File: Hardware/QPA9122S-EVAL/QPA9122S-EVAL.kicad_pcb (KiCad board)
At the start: 2 copper layers, 58.5 x 27.9 mm, 15 parts, among them IC1 QPA9122TR7, J1 Conn_Coaxial, J2 Conn_Coaxial

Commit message: Power distribution
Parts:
- added J3: Conn_01x02_Pin, Connector_PinHeader_1.00mm:PinHeader_1x02_P1.00mm_Vertical, F.Cu at (122.2, 83.0)
- added J4: Conn_01x02_Pin, Connector_PinHeader_1.00mm:PinHeader_1x02_P1.00mm_Vertical, F.Cu at (114.9, 107.1)
- added J5: Conn_01x02_Pin, Connector_PinHeader_1.00mm:PinHeader_1x02_P1.00mm_Vertical, F.Cu at (113.8, 83.1)
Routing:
- net V_PD: track 0.00 -> 8.58 mm
- net VCC: track 7.41 -> 15.5 mm
- net VCC1: track 2.81 -> 9.59 mm
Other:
- board text added: "+1.8V"
- board text added: "+5V"
- board text added: "GND"

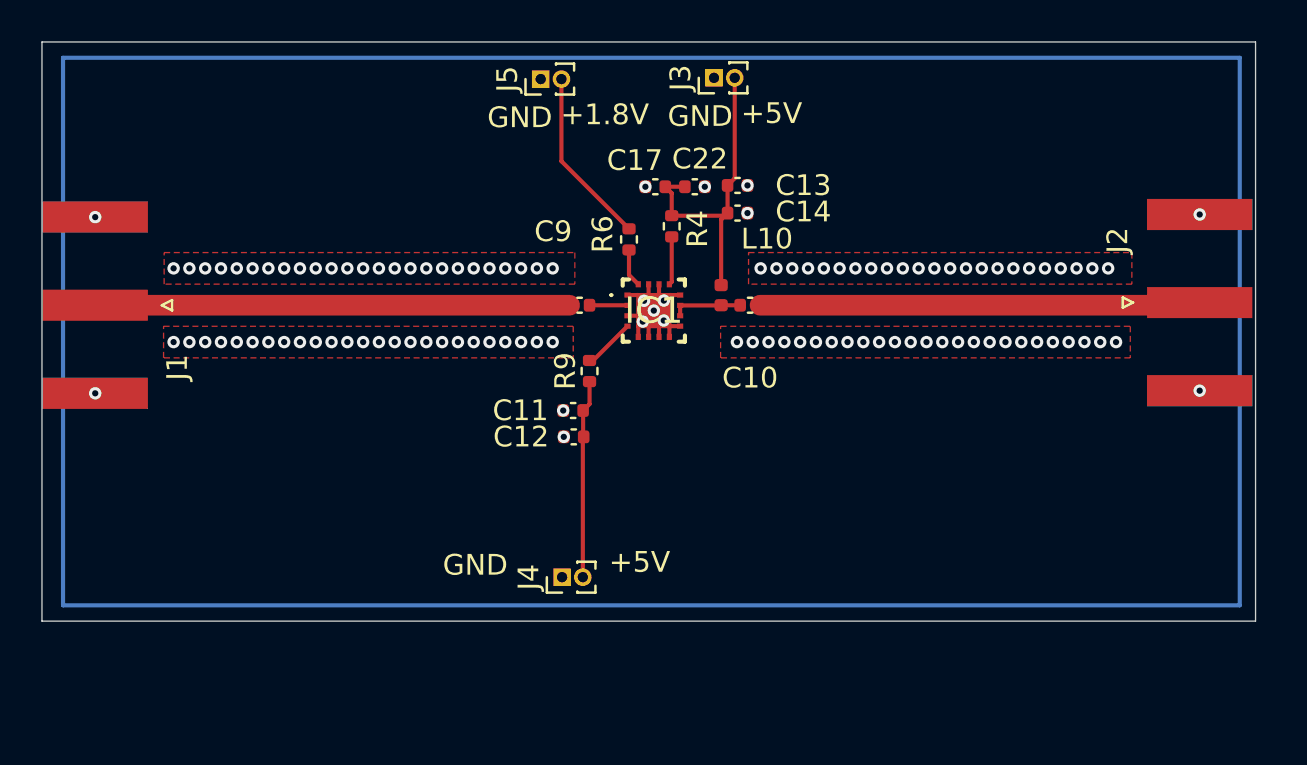
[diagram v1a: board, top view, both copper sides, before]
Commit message: Added T-line test point and better labeling.
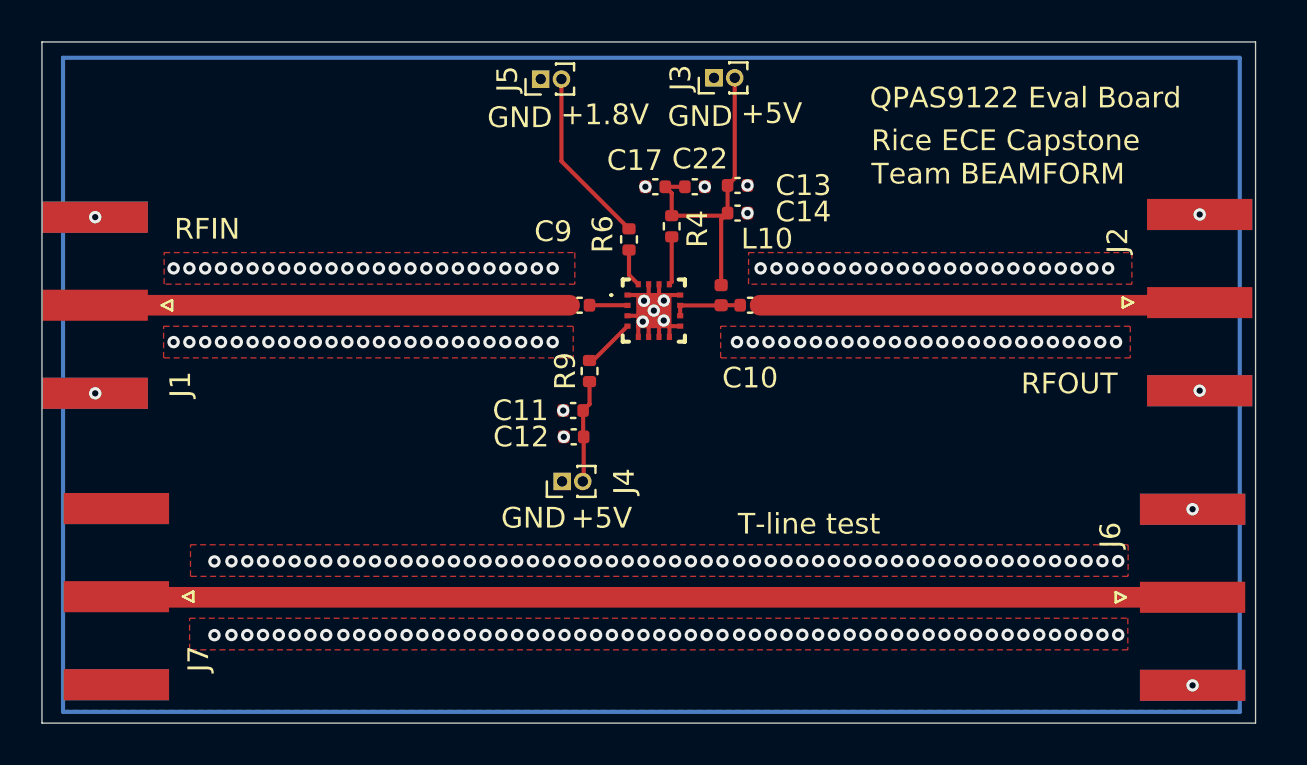
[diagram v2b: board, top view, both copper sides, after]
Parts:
- added J6: Conn_Coaxial, Connector_Coaxial:SMA_Amphenol_132289_EdgeMount, F.Cu at (145.3, 108.1)
- added J7: Conn_Coaxial, Connector_Coaxial:SMA_Amphenol_132289_EdgeMount, F.Cu at (93.4, 108.0)
- moved J4 4.62 mm to (114.9, 102.5)
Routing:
- net Net-(J6-In): track 0.00 -> 51.9 mm
- net VCC1: track 9.59 -> 5.03 mm
- net GND: vias 113 -> 231
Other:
- board size 58.5 x 27.9 mm -> 58.5 x 32.9 mm
- board text added: "QPAS9122 Eval Board"
- board text added: "RFIN"
- board text added: "RFOUT"
- board text added: "Rice ECE Capstone Team BEAMFORM"
- board text added: "T-line test"

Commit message: DRC fixes
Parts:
- moved J1 0.63 mm to (93.0, 94.0)
- moved J2 0.44 mm to (145.2, 93.9)
- moved J6 0.16 mm to (145.1, 108.1)
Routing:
- net GND: vias 231 -> 233
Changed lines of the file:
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@@
 	)
 	(setup
+		(stackup
+			(layer "F.SilkS"
+				(type "Top Silk Screen")
+			)
+			(layer "F.Paste"
+				(type "Top Solder Paste")
+			)
+			(layer "F.Mask"
+				(type "Top Solder Mask")
+				(thickness 0.01)
+			)
+			(layer "F.Cu"
+				(type "copper")
+				(thickness 0.035)
+			)
+			(layer "dielectric 1"
+				(type "core")
+				(thickness 1.51)
+				(material "FR4")
+				(epsilon_r 4.5)
+				(loss_tangent 0.02)
+			)
+			(layer "B.Cu"
+				(type "copper")
+				(thickness 0.035)
+			)
+			(layer "B.Mask"
+				(type "Bottom Solder Mask")
+				(thickness 0.01)
+			)
+			(layer "B.Paste"
+				(type "Bottom Solder Paste")
+			)
+			(layer "B.SilkS"
+				(type "Bottom Silk Screen")
+			)
+			(copper_finish "None")
+			(dielectric_constraints no)
+		)
 		(pad_to_mask_clearance 0)
 		(allow_soldermask_bridges_in_footprints no)
@@
 	(footprint "Connector_Coaxial:SMA_Amphenol_132289_EdgeMount"
 		(layer "F.Cu")
-		(at 145.6405 93.853)
+		(at 145.1975 93.89)
 		(descr "https://www.amphenolrf.com/library/download/link/link_id/595984/parent/132289/")
 		(tags "SMA")
@@
 	(footprint "Connector_Coaxial:SMA_Amphenol_132289_EdgeMount"
 		(layer "F.Cu")
-		(at 92.3575 93.98 180)
+		(at 92.9825 93.96 180)
 		(descr "https://www.amphenolrf.com/library/download/link/link_id/595984/parent/132289/")
 		(tags "SMA")
@@
 	(footprint "Connector_Coaxial:SMA_Amphenol_132289_EdgeMount"
 		(layer "F.Cu")
-		(at 145.2975 108.07)
+		(at 145.1375 108.09)
 		(descr "https://www.amphenolrf.com/library/download/link/link_id/595984/parent/132289/")
 		(tags "SMA")
@@
 	(gr_rect
 		(start 90.805 82.042)
-		(end 147.574 113.598)
+		(end 147.574 113.31)
 		(stroke
 			(width 0.2)
@@
 	)
 	(via
-		(at 145.6405 89.603)
+		(at 145.1975 89.64)
 		(size 0.6)
 		(drill 0.3)
@@
 	)
 	(via
-		(at 145.6405 98.103)
+		(at 145.1975 98.14)
 		(size 0.6)
 		(drill 0.3)
@@
 	)
 	(via
+		(at 93.38 103.79)
+		(size 0.6)
+		(drill 0.3)
+		(layers "F.Cu" "B.Cu")
+		(net 5)
+	)
+	(via
 		(at 140.462 92.202)
 		(size 0.6)
@@
 	)
 	(via
+		(at 93.38 112.29)
+		(size 0.6)
+		(drill 0.3)
+		(layers "F.Cu" "B.Cu")
+		(net 5)
+	)
+	(via
 		(at 127.889 95.758)
 		(size 0.6)
@@
 		(polygon
 			(pts
-				(xy 147.574 82.042) (xy 90.805 82.042) (xy 90.805 113.528) (xy 147.574 113.528)
+				(xy 147.574 82.042) (xy 90.805 82.042) (xy 90.805 113.528) (xy 147.574 113.31)
 			)
 		)
